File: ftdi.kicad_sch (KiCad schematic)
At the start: 37 parts, among them U2301 NCP718BSN330T1G, U2302 TXU0304BQAR, U2303 FT4232H_VQFN, U2304 TXU0304BQAR, Y2301 Resonator_12MHz_ABM8G

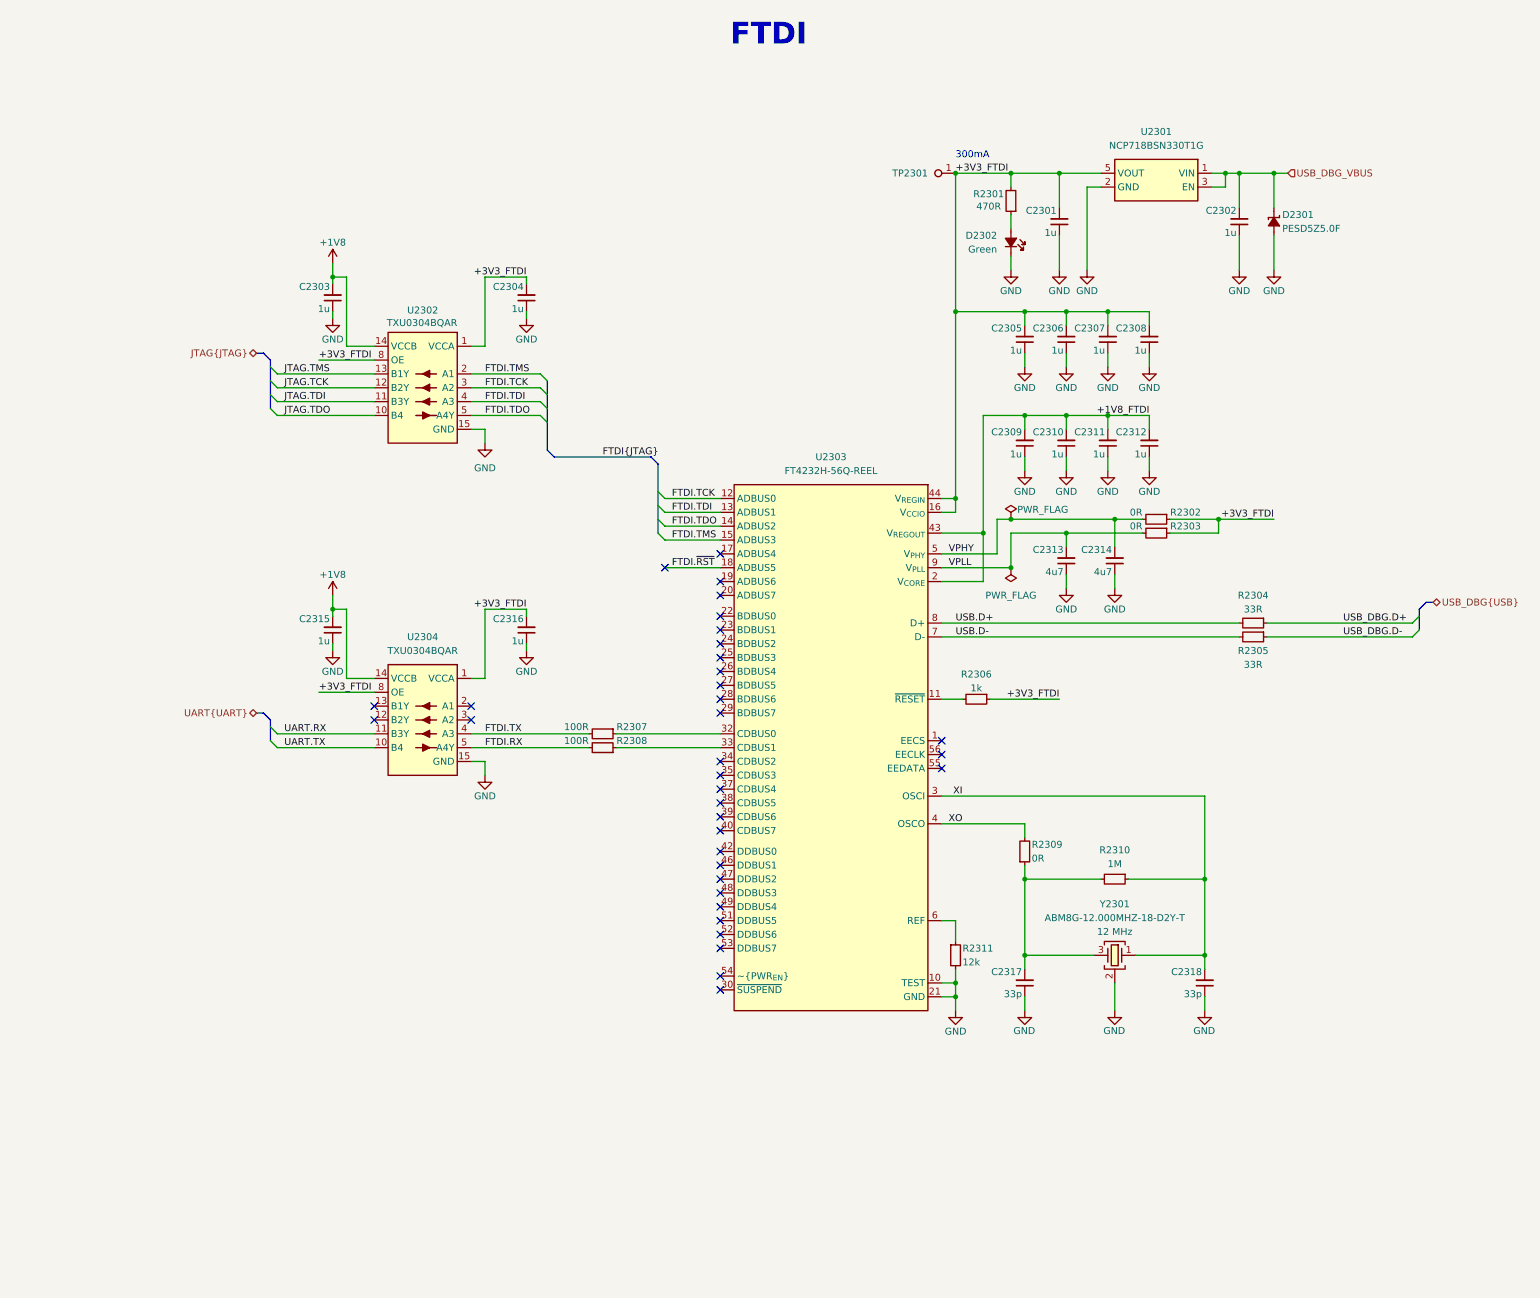
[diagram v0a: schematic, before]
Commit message: [#100282] Add missing schematic sheet names and align them all
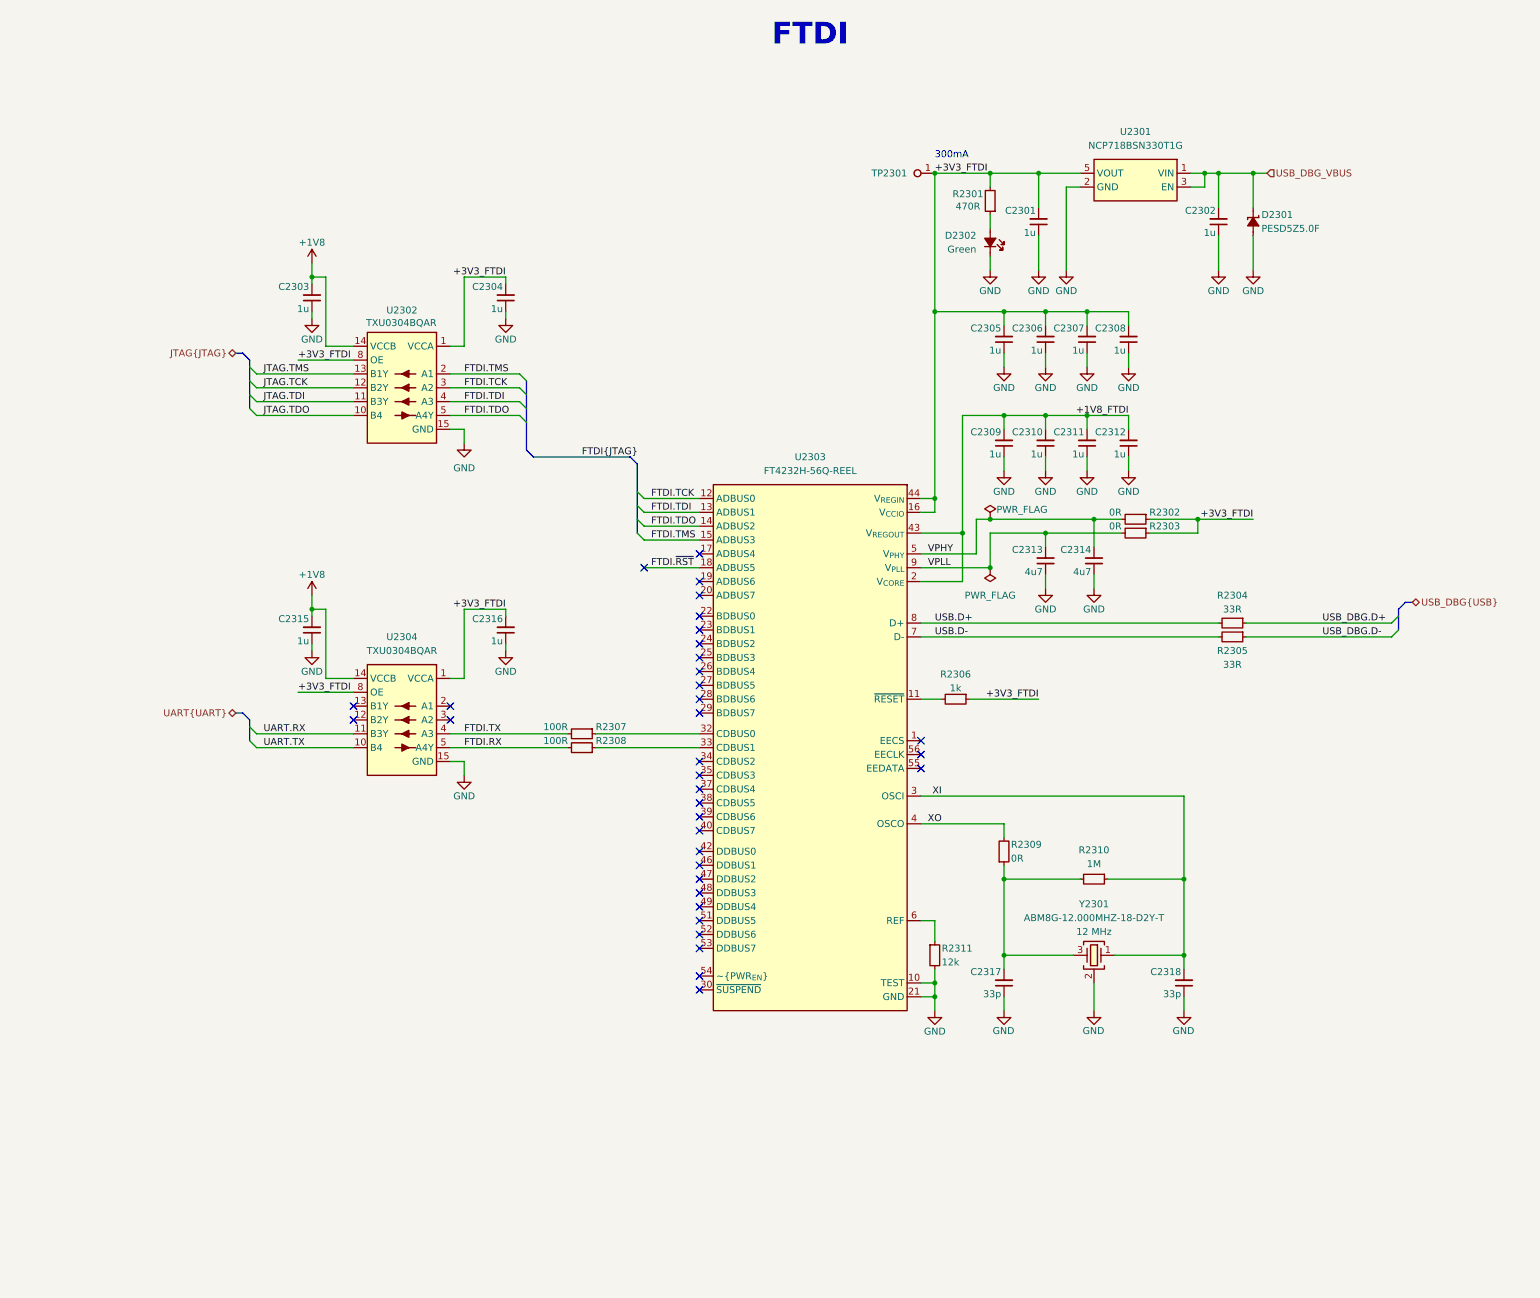
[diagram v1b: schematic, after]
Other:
- moved on the sheet: C2301, C2302, C2303, C2304, C2305, C2306, C2307, C2308, C2309, C2310, C2311, C2312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

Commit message: [#100501] Reannotate schematic
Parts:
- renumbered C2301 to C225, C2302 to C226, C2303 to C227, C2304 to C228, C2305 to C229, C2306 to C230, C2307 to C231, C2308 to C232, C2309 to C233, C2310 to C234, C2311 to C235, C2312 to C236, C2313 to C237, C2314 to C238, C2315 to C239, C2316 to C240, C2317 to C241, C2318 to C242, D2301 to D13, D2302 to D14, R2301 to R295, R2302 to R296, R2303 to R297, R2304 to R298, R2305 to R299, R2306 to R300, R2307 to R301, R2308 to R302, R2309 to R303, R2310 to R304, R2311 to R305, TP2301 to TP29, U2301 to U40, U2302 to U41, U2303 to U42, U2304 to U43, Y2301 to Y6

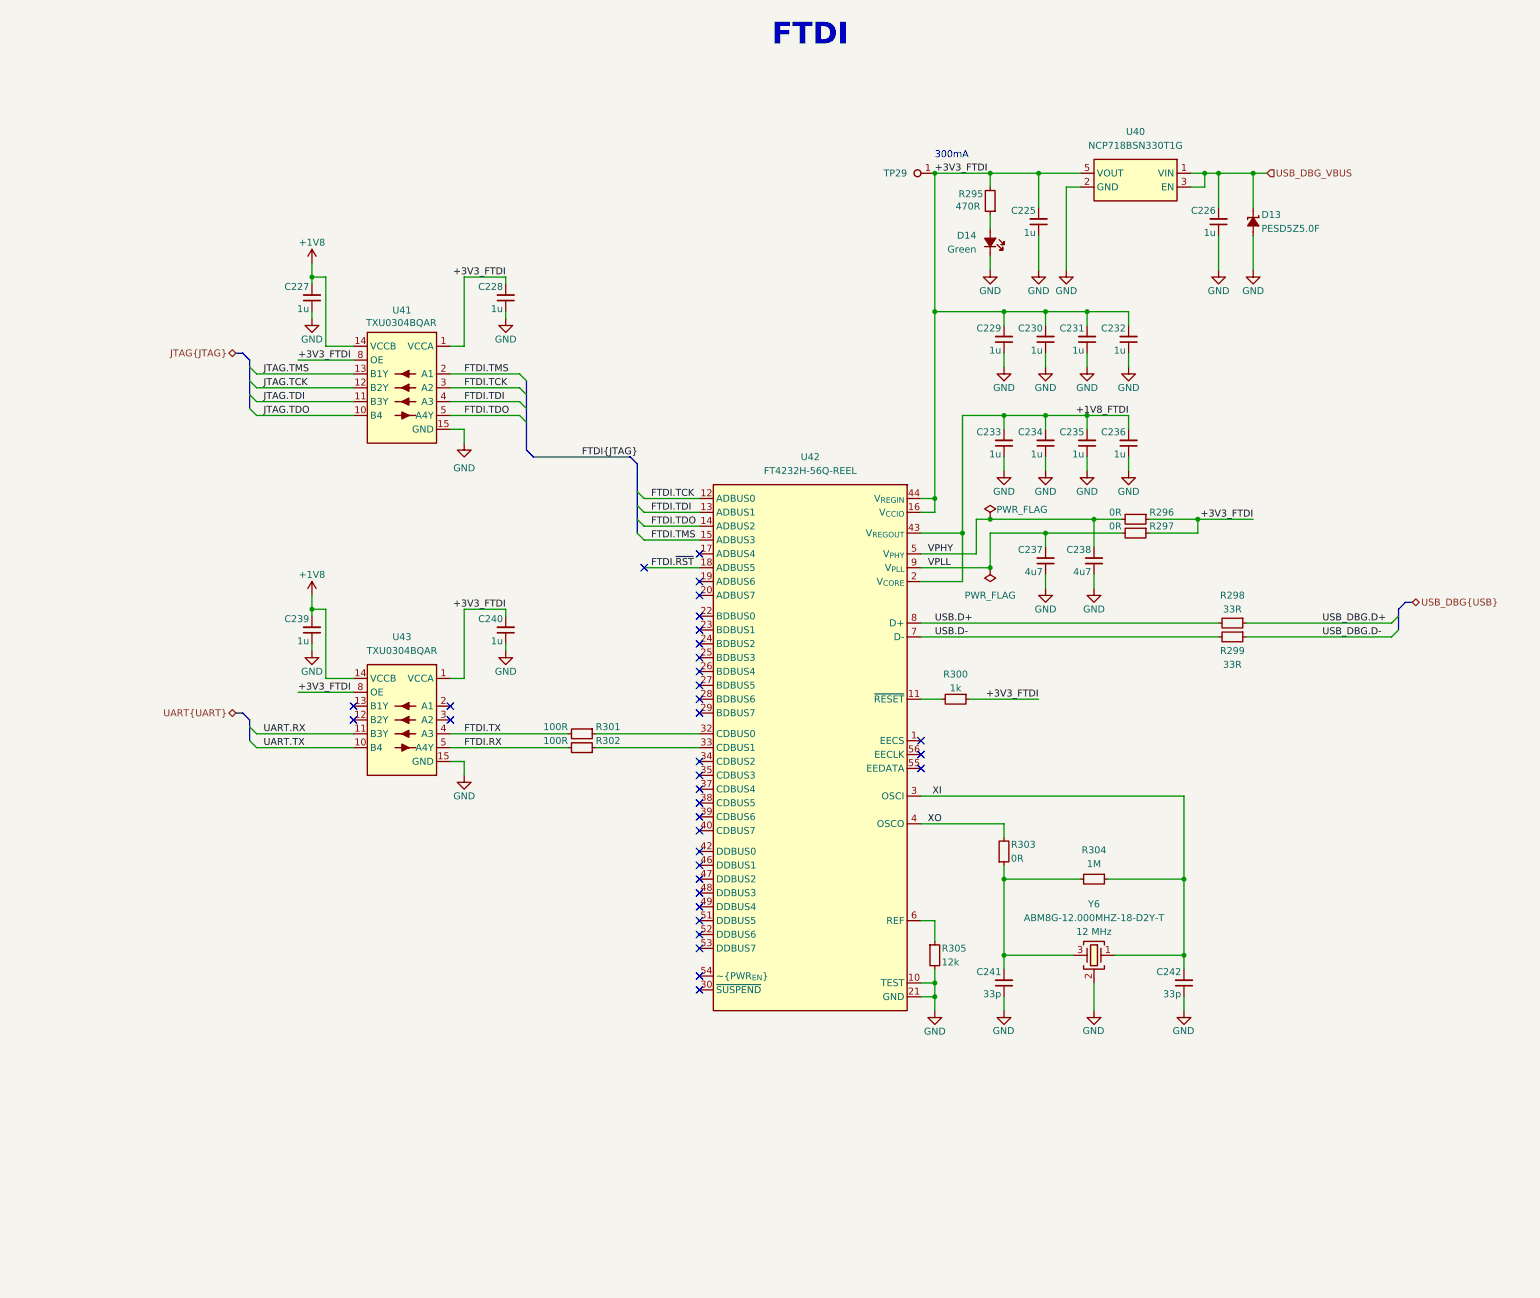
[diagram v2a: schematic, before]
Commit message: [#100501] Add Tag-Connect to JTAG and config EEPROM to FTDI, connect DC-SCM USB1 to USB controller
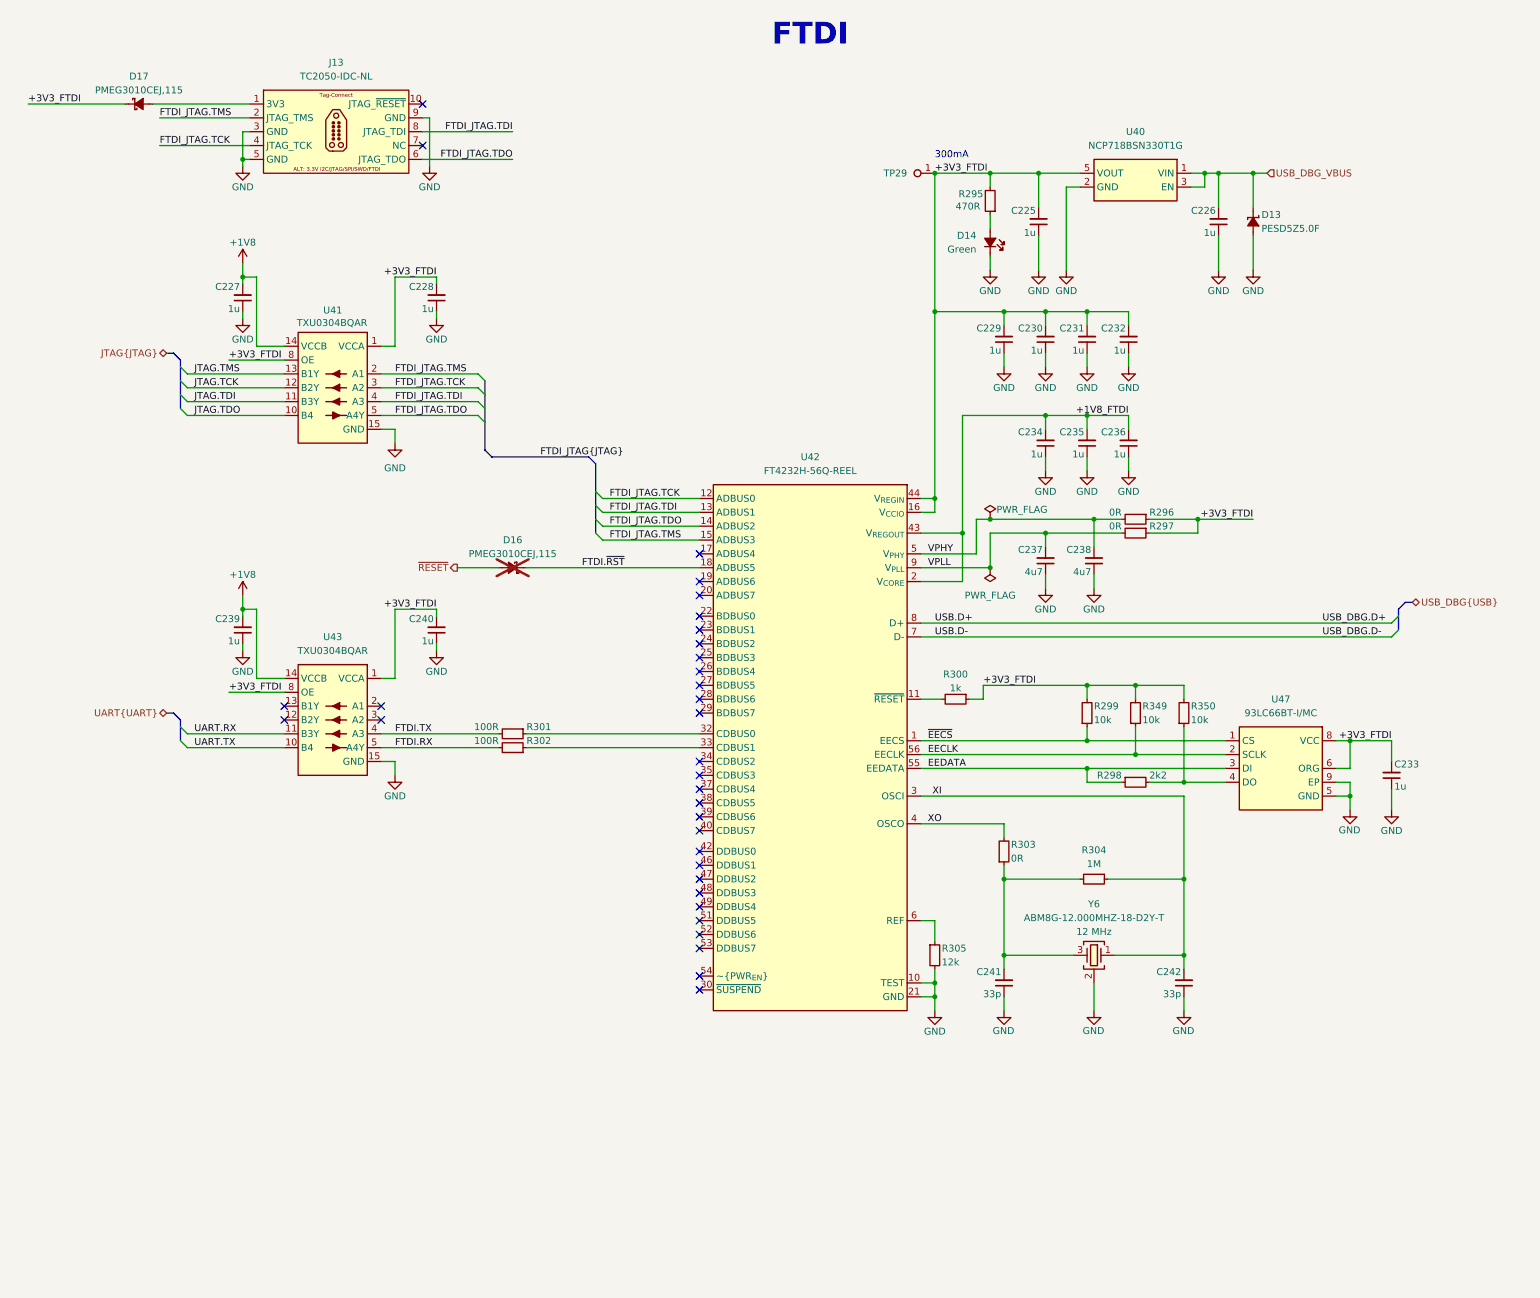
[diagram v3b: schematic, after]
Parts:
- removed R298, R299: R_33R_0402, antmicro-footprints:R_0402_1005Metric, symbol antmicroResistors0402:R_33R_0402
- added D16, D17: PMEG3010CEJ,115, antmicro-footprints:D_SOD-323F, symbol antmicroDiodesRectifiersSingle:PMEG3010CEJ,115
- added J13: Tag-Connect_TC2050-IDC-NL_2x5_P1.27mm, antmicro-footprints:Tag-Connect_TC2050-IDC-NL_2x5_P1.27mm, symbol antmicroTestPoints:Tag-Connect_TC2050-IDC-NL_2x5_P1.27mm
- added R298: R_2k2_0402, antmicro-footprints:R_0402_1005Metric, symbol antmicroResistors0402:R_2k2_0402
- added R299, R349, R350: R_10k_0402, antmicro-footprints:R_0402_1005Metric, symbol antmicroResistors0402:R_10k_0402
- added U47: 93LC66BT_DFN, antmicro-footprints:DFN-8-1EP_3x2mm_P0.5mm_EP1.36x1.46mm, symbol antmicroMemory:93LC66BT_DFN
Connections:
- net +1V8_FTDI: no longer C233.2
- net +3V3_FTDI: now also C233.2, D17.1 (C), R299.2, R349.2, R350.2, U47.6 (ORG), U47.8 (VCC)
- net FTDI.~{RST}: now also D16.1 (C)
- net GND: now also J13.3, J13.5, J13.9, U47.5 (GND), U47.9 (EP)
- net ~{EECS}: now reaches U42.1 (EECS)
- net ~{EECS}: now also R299.1, U47.1 (CS)
- net EEDATA: now reaches U42.55 (EEDATA)
- net EEDATA: now also R298.1, U47.3 (DI)
- net EECLK: now reaches U42.56 (EECLK)
- net EECLK: now also R349.1, U47.2 (SCLK)
- net FTDI.TCK renamed FTDI_JTAG.TCK
- net FTDI_JTAG.TCK: now also J13.4
- net FTDI.TDI renamed FTDI_JTAG.TDI
- net FTDI_JTAG.TDI: now also J13.8
- net FTDI.TDO renamed FTDI_JTAG.TDO
- net FTDI_JTAG.TDO: now also J13.6
- net FTDI.TMS renamed FTDI_JTAG.TMS
- net FTDI_JTAG.TMS: now also J13.2
- new net: R298.2, R350.1, U47.4 (DO)
- new net: D17.2 (A), J13.1
- new net ~{RESET}: D16.2 (A)
- no-connect marks 35 -> 33
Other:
- moved on the sheet: C227, C228, C239, C240, R301, R302, U41, U43

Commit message: [#100501] Clean ERC
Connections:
- net USB.D+ renamed USB_DBG.D+
- net USB.D- renamed USB_DBG.D-
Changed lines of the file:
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@@
-		)
-	)
-	(label "USB.D-"
-		(at 233.68 148.59 0)
-		(effects
-			(font
-				(size 1.27 1.27)
-			)
-			(justify left bottom)
 		)
 	)
@@
 		(effects
 			(font
-				(size 1.27 1.27)
-			)
-			(justify left bottom)
-		)
-	)
-	(label "USB.D+"
-		(at 233.68 146.05 0)
-		(effects
-			(font

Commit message: [#100501] Add FTDI RX/TX LEDs
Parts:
- added C105: C_100n_0402, antmicro-footprints:C_0402_1005Metric, symbol antmicroCapacitors0402:C_100n_0402
- added D24, D25, D26, D27: LED_G_0402_VLMTG1500-GS08, antmicro-footprints:LED_0402_1005Metric_G, symbol antmicroLEDIndicationDiscrete:LED_G_0402_VLMTG1500-GS08
- added R224, R356, R365, R366, R372: R_10k_0402, antmicro-footprints:R_0402_1005Metric, symbol antmicroResistors0402:R_10k_0402
- added U19: SN74HC595B, antmicro-footprints:X1QFN-16-1EP_2.5x2.5mm, symbol antmicroLogicShiftRegisters:SN74HC595B
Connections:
- net +3V3_FTDI: now also C105.2, R224.1, U19.10 (~{SRCLR}), U19.16 (VCC)
- net EECLK: now also U19.11 (SRCLK)
- net EEDATA: now also U19.14 (SER)
- net GND: now also C105.1, D24.1 (C), D25.1 (C), D26.1 (C), D27.1 (C), U19.8 (GND)
- net ~{EECS}: now also U19.12 (RCLK)
- net FTDI_PWREN: now reaches U42.54 (~{PWR_{EN}})
- net FTDI_PWREN: now also R224.2, U19.13 (~{OE})
- new net: D26.2 (A), R366.2
- new net: D25.2 (A), R356.2
- new net: D24.2 (A), R365.2
- new net: D27.2 (A), R372.2
- new net LED_RX0: R365.1, U19.5 (QF)
- new net LED_RX1: R372.1, U19.7 (QH)
- new net LED_TX0: R356.1, U19.4 (QE)
- new net LED_TX1: R366.1, U19.6 (QG)
- no-connect marks 33 -> 37

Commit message: [#100501] Reannotate schematic
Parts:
- renumbered C225 to C216, C226 to C217, C227 to C218, C228 to C219, C229 to C220, C230 to C221, C231 to C222, C232 to C223, C234 to C224, C235 to C225, C236 to C226, C237 to C227, C238 to C228, C239 to C229, C240 to C230, C233 to C231, C241 to C232, C242 to C233, C105 to C234, D17 to D18, D13 to D19, D14 to D20, D16 to D21, D25 to D22, D24 to D23, D26 to D24, D27 to D25, J13 to J12, R295 to R320, R296 to R321, R297 to R322, R300 to R323, R299 to R324, R349 to R325, R350 to R326, R301 to R327, R302 to R328, R298 to R329, R303 to R330, R304 to R331, R305 to R332, R224 to R333, R356 to R334, R365 to R335, R366 to R336, R372 to R337, TP29 to TP35, U40 to U37, U41 to U38, U42 to U39, U43 to U40, U47 to U41, U19 to U42

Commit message: [#100501] Perform minor BOM consolidation
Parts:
- removed D19: PESD5Z5_0F, antmicro-footprints:SOD-523, symbol antmicroTVSDiodes:PESD5Z5_0F
- added D27: PESD5V0X1UB, antmicro-footprints:SOD-523, symbol antmicroTVSDiodes:PESD5V0X1UB
- C216, C217, C218, C219, C220, C221, C222, C223, C224, C225, C226, C229, C230, C231: value C_1u_0402 -> C_1u_25V_0402; symbol antmicroCapacitors0402:C_1u_0402 -> antmicroCapacitors0402:C_1u_25V_0402; Dielectric (none) -> X5R; MPN C1005X6S1A105K050BC -> GRM155R61E105KE11J; Manufacturer TDK -> Murata; Voltage (none) -> 25V
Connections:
- net GND: now also D27.2 (A)
- net USB_DBG_VBUS: now also D27.1 (C)
